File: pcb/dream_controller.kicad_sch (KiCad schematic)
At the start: 5 parts

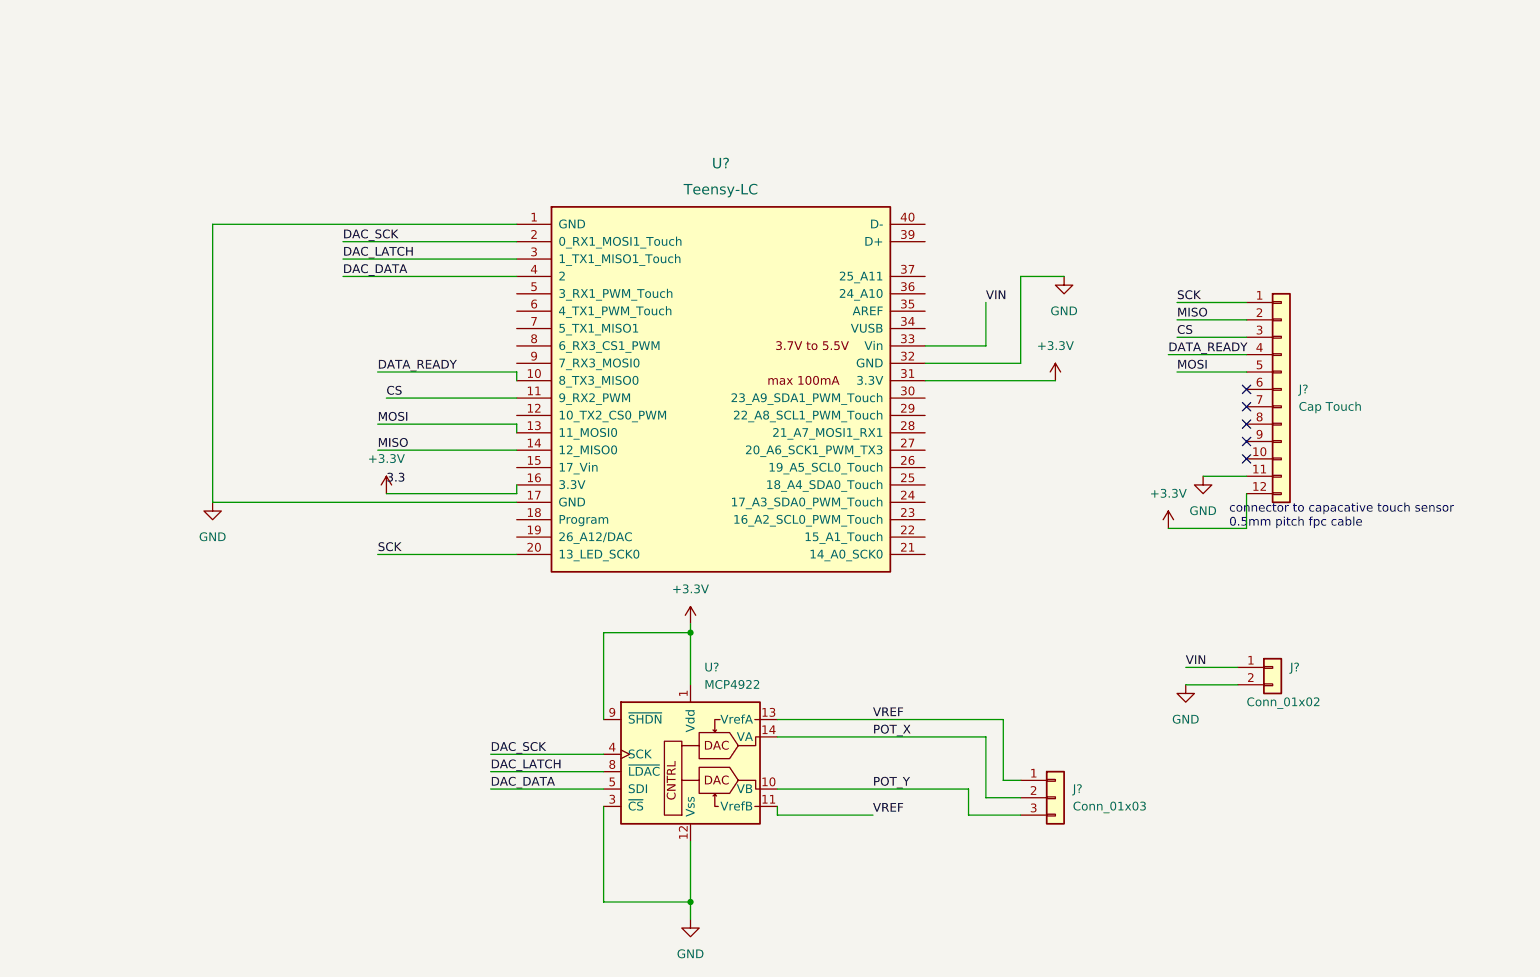
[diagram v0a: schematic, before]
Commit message: Clean up schematic
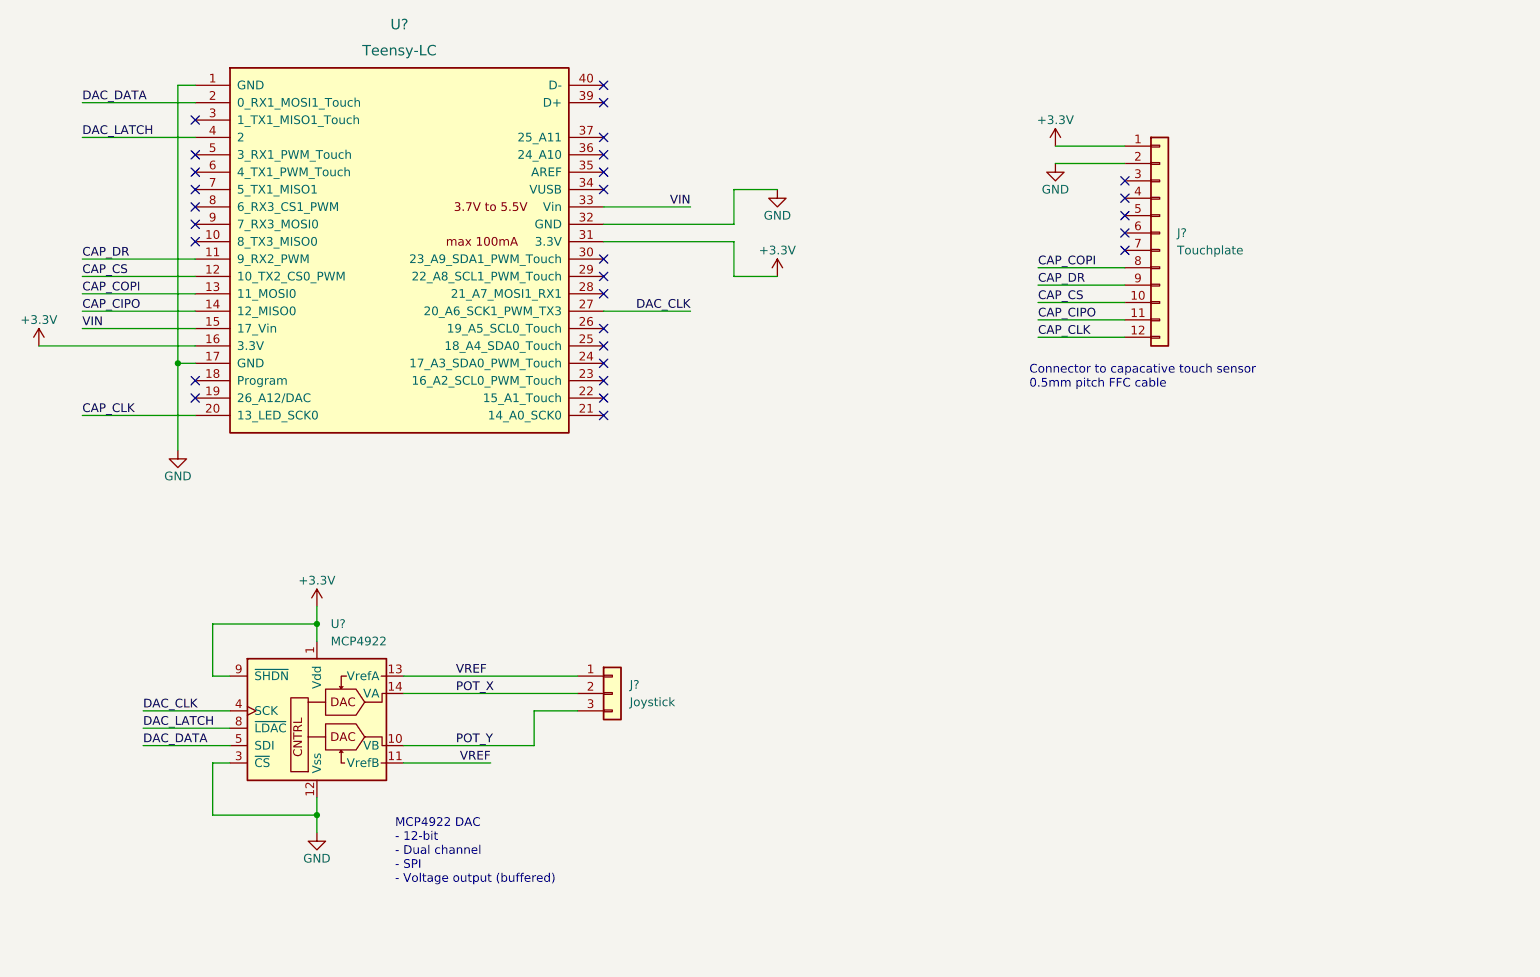
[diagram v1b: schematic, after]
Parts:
- removed J?: Conn_01x02, symbol Connector_Generic:Conn_01x02
- J?: value Cap Touch -> Touchplate
- J?: value Conn_01x03 -> Joystick
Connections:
- net +3V3: now also J?.1 (Pin_1); no longer J?.12 (Pin_12)
- net DAC_DATA: now also U?.2 (0_RX1_MOSI1_Touch); no longer U?.4 (2)
- net DAC_LATCH: now also U?.4 (2); no longer U?.3 (1_TX1_MISO1_Touch)
- net GND: now also J?.2 (Pin_2); no longer J?.11 (Pin_11)
- net VIN: now also U?.15 (17_Vin)
- net CAP_CS: now reaches J?.10 (Pin_10)
- net CAP_CS: now also U?.12 (10_TX2_CS0_PWM)
- net CAP_COPI: now reaches J?.8 (Pin_8)
- net CAP_COPI: now also U?.13 (11_MOSI0)
- net CAP_DR: now reaches J?.9 (Pin_9)
- net CAP_DR: now also U?.11 (9_RX2_PWM)
- net DAC_CLK: now reaches U?.27 (20_A6_SCK1_PWM_TX3)
- net DAC_CLK: now also U?.4 (SCK)
- net CS: no longer names the net of J?.3 (Pin_3)
- net CS: no longer U?.11 (9_RX2_PWM)
- removed net DAC_SCK: U?.2 (0_RX1_MOSI1_Touch), U?.4 (SCK)
- net DATA_READY: no longer names the net of J?.4 (Pin_4)
- net DATA_READY: no longer U?.10 (8_TX3_MISO0)
- net MISO renamed CAP_CIPO
- net CAP_CIPO: now also J?.11 (Pin_11); no longer J?.2 (Pin_2)
- net MOSI: no longer names the net of J?.5 (Pin_5)
- net MOSI: no longer U?.13 (11_MOSI0)
- net SCK renamed CAP_CLK
- net CAP_CLK: now also J?.12 (Pin_12); no longer J?.1 (Pin_1)
- no-connect marks 5 -> 29
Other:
- note added: "Connector to capacative touch sensor 0.5mm pitch FFC cable"
- note added: "MCP4922 DAC - 12-bit - Dual channel - SPI - Voltage output (buffered)"
- note removed: "connector to capacative touch sensor 0.5mm pitch fpc cable"
- moved on the sheet: J?, U?

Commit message: uwu pogchamp
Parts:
- J1: renamed from J?; footprint (none) -> Dream Controller:TE Connectivity 12P0.5mm FPC
- J2: renamed from J?; footprint (none) -> Connector_PinHeader_2.00mm:PinHeader_1x03_P2.00mm_Vertical
- U1: renamed from U?; footprint (none) -> teensy:Teensy_LC
- U2: renamed from U?; footprint (none) -> Package_SO:TSSOP-14_4.4x5mm_P0.65mm
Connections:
- net +3V3: no longer U1.16 (3.3V)
- net GND: no longer U1.17 (GND)
- net VIN: no longer U1.15 (17_Vin)
- no-connect marks 29 -> 32

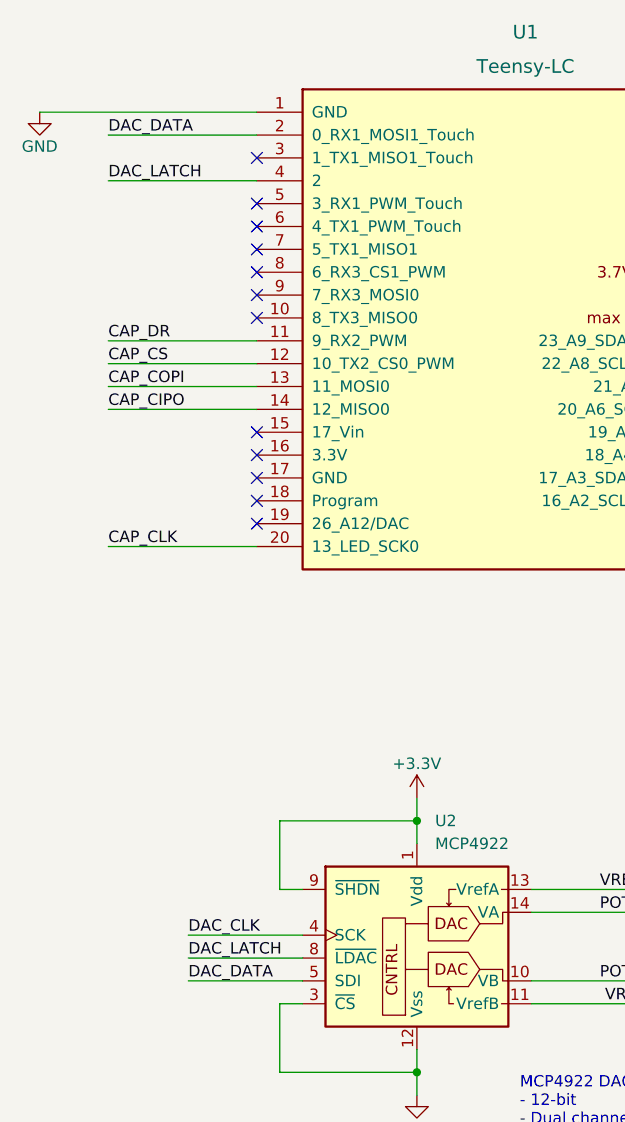
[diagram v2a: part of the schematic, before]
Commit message: Get DAC working
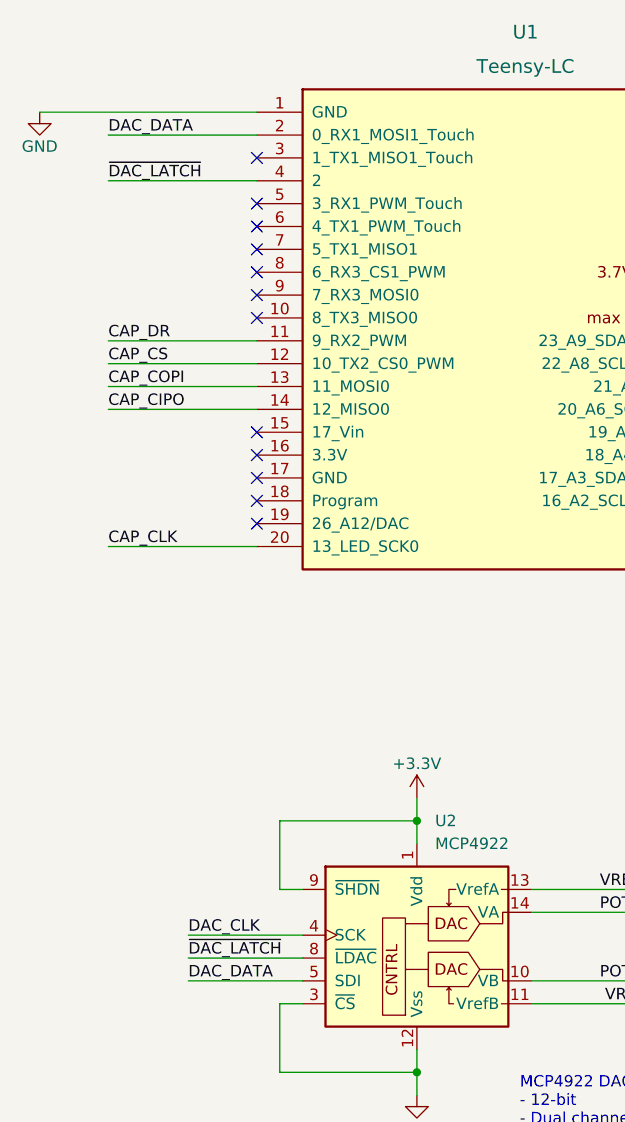
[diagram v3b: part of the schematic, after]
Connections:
- net DAC_LATCH renamed ~{DAC_LATCH}
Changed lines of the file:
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@@
     (effects (font (size 1.27 1.27)) (justify left bottom))
   )
-  (label "DAC_LATCH" (at 53.34 60.96 0)
+  (label "~{DAC_LATCH}" (at 53.34 60.96 0)
     (effects (font (size 1.27 1.27)) (justify left bottom))
   )
-  (label "DAC_LATCH" (at 62.23 147.32 0)
+  (label "~{DAC_LATCH}" (at 62.23 147.32 0)
     (effects (font (size 1.27 1.27)) (justify left bottom))
   )
